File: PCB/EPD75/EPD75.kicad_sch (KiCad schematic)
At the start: 109 parts, among them J1 Conn_01x26, J10 TF_PUSH, J11 Reset, J12 TC2030-USB-NL-DS, J3 RELAY, J4 BTN1, J5 USB-C-Socket-V, J6 BTN2, J7 USB-C-Socket-V, J8 PWR, Q1 BSS138, U2 ESP32-S3-MINI-1, U3 MD8942, U8 G3VM-41GR8

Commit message: Clean up
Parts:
- added R15, R16, R17: 10K, RevK:R_0402, symbol Device:R
- R1: LCSC Part # (none) -> C2771738
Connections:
- net +3.3V: now also R15.1, R16.1, R17.1
- net SDMISO: now also R17.2
- net SDMOSI: now also R16.2
- net SDSCK: now also R15.2

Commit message: Resistors
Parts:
- added R18, R19, R20: 10K, RevK:R_0402, symbol Device:R
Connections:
- net +3.3V: now also R18.1, R19.1, R20.1
- net SDMISO: now also R19.2; no longer R17.2
- net SDSCK: now also R18.2; no longer R15.2
- net SDSS: now also R15.2
- net at J10.1 (DAT2): now also R17.2
- net at J10.8 (DAT1): now also R20.2
- no-connect marks 27 -> 25
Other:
- moved on the sheet: J10, R17

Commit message: Tidy
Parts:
- added R21: 10K, RevK:R_0402, symbol Device:R
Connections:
- net +3.3V: now also R21.1
- net SDCD: now also R21.2
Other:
- moved on the sheet: J10, R15, R16, R17, R18, R19, R20

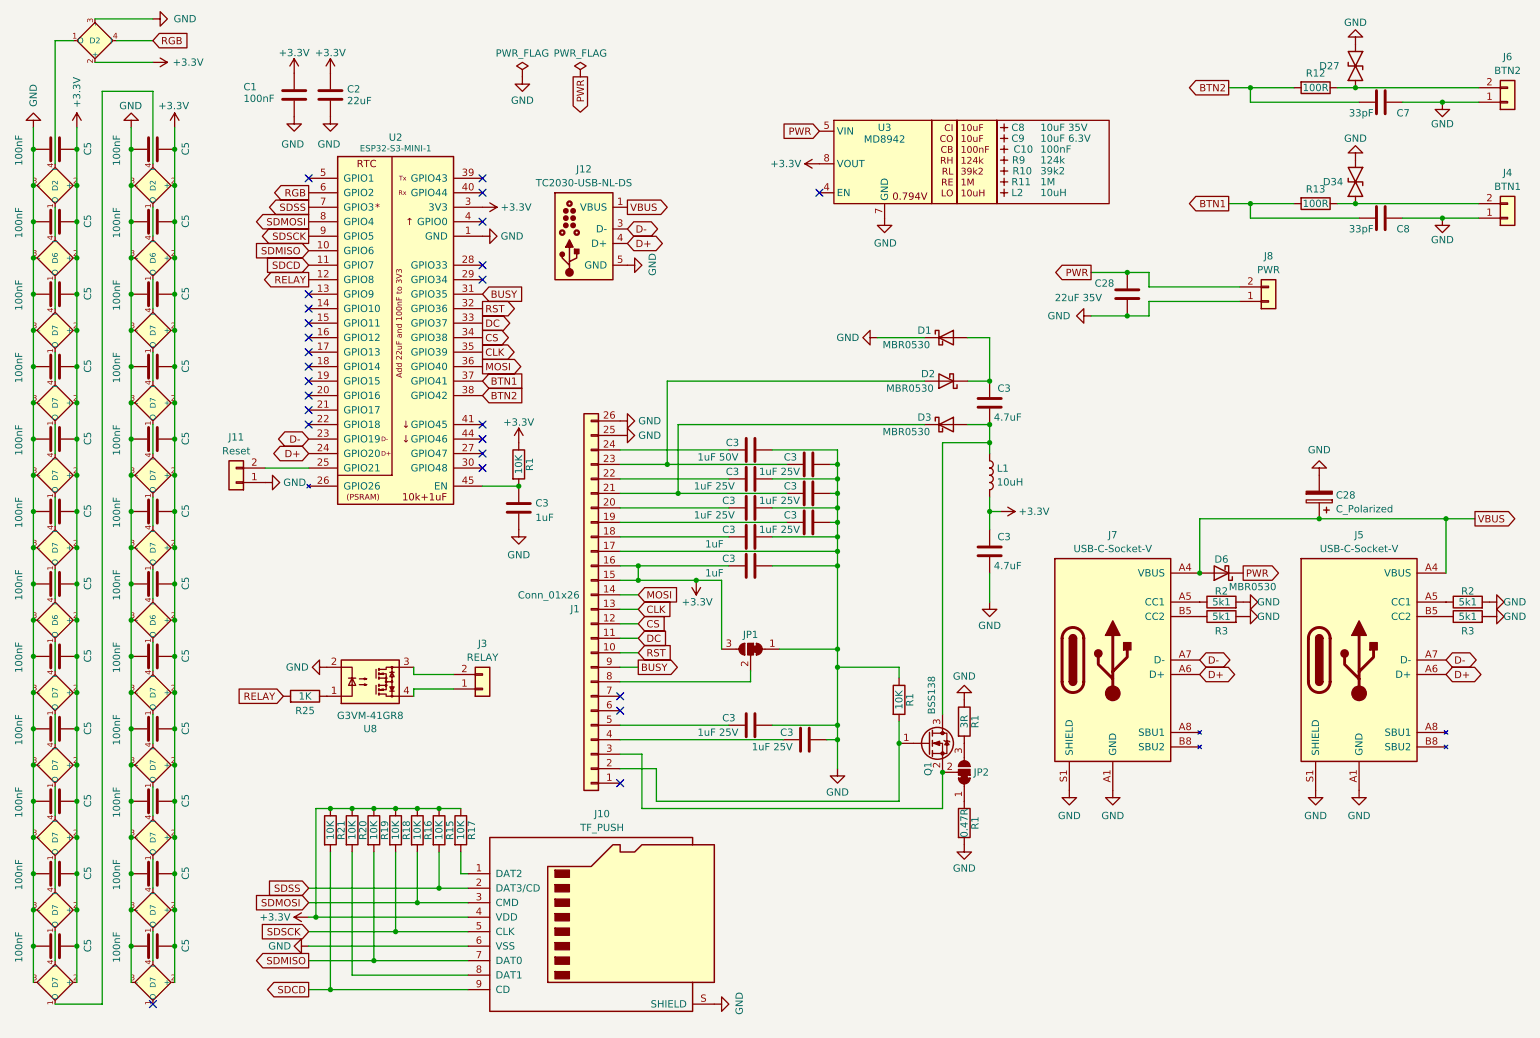
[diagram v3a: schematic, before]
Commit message: New SD card wiring
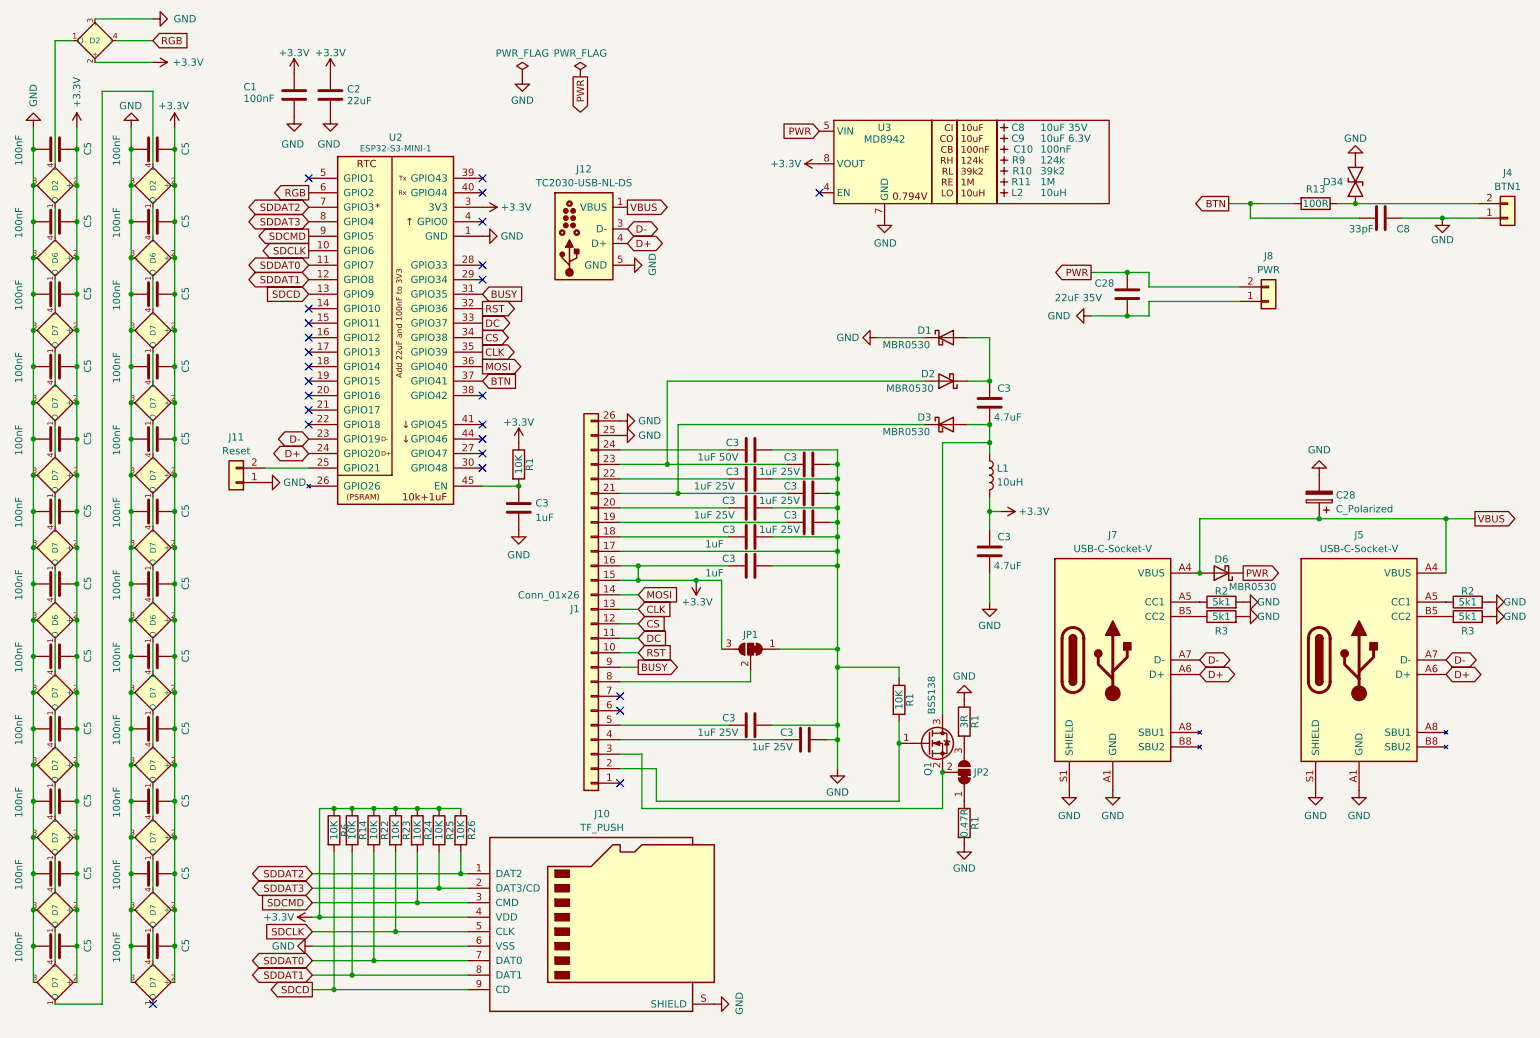
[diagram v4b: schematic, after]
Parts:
- removed C7: 33pF, RevK:C_0402, symbol Device:C
- removed D27: ~, RevK:DFN1006-2L, symbol RevK:ES05D1MC10
- removed J3: RELAY, RevK:WAGO-2060-452-998-404, symbol Connector_Generic:Conn_01x02
- removed J6: BTN2, RevK:WAGO-2060-452-998-404, symbol Connector_Generic:Conn_01x02
- removed R12: 100R, RevK:R_0402, symbol Device:R
- removed R15, R16, R17, R18, R19, R20, R21: 10K, RevK:R_0402, symbol Device:R
- removed U8: G3VM-41GR8, RevK:Special-SOP-4-3.7x4.55, symbol RevK:G3VM-41GR8
- added R14, R22, R23, R24, R26, R6: 10K, RevK:R_0402, symbol Device:R
- R25: value 1K -> 10K
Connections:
- net +3.3V: now also R25.1, R14.1, R22.1, R23.1, R24.1, R26.1, R6.1
- net SDCD: now also U2.13 (GPIO9), R6.2; no longer U2.11 (GPIO7)
- net SDDAT2: now reaches J10.1 (DAT2)
- net SDDAT2: now also U2.7 (GPIO3), R26.2
- net SDDAT1: now reaches J10.8 (DAT1)
- net SDDAT1: now also U2.12 (GPIO8), R14.2
- net BTN1 renamed BTN
- net BTN2: no longer names the net of U2.38 (GPIO42)
- net RELAY renamed SDDAT3
- net SDDAT3: now also J10.2 (DAT3/CD), U2.8 (GPIO4); no longer U2.12 (GPIO8)
- net SDMISO renamed SDCLK
- net SDCLK: now also J10.5 (CLK), R23.2; no longer J10.7 (DAT0)
- net SDMOSI renamed SDCMD
- net SDCMD: now also U2.9 (GPIO5), R24.2; no longer U2.8 (GPIO4)
- removed net SDSCK: J10.5 (CLK), U2.9 (GPIO5)
- removed net SDSS: J10.2 (DAT3/CD), U2.7 (GPIO3)
- new net SDDAT0: J10.7 (DAT0), R22.2, U2.11 (GPIO7)

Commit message: Tidy
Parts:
- D10, D11, D12, D15, D16, D17, D18, D19, D23, D24, D25, D26, D29, D30, D31, D32, D33, D9: renamed from D7; footprint RevK:SMD1010 -> (none); LCSC Part # C5349953 -> (none); MPN (none) -> C5349953
- D14, D22, D28, D8: renamed from D6; footprint RevK:SMD1010 -> (none); LCSC Part # C5349953 -> (none); MPN (none) -> C5349953
- D21, D35, D5: renamed from D2; footprint RevK:SMD1010 -> (none); LCSC Part # C5349953 -> (none); MPN (none) -> C5349953
- D34: LCSC Part # C5137770 -> (none); MPN (none) -> C5137770
- J10: LCSC Part # C393941 -> (none); MPN (none) -> C393941; Position Offset (none) -> 0,0.15
- J5, J7: LCSC Part # C709357 -> (none); MPN (none) -> C709357; Position Offset (none) -> 0,0.715
- Q1: JLCPCB Rotation Offset 180 -> (none); LCSC Part # C2938375 -> (none); MPN (none) -> C2938375; Rotation Offset (none) -> 180
- U3: LCSC Part # C2684786 -> (none); MPN (none) -> C2684786; Rotation Offset (none) -> 180
- U4: renamed from U2; LCSC Part # C3013941 -> (none); MPN (none) -> C3013941
- renumbered C3 to C1, C3 to C11, C3 to C12, C3 to C13, C3 to C14, C3 to C15, C3 to C16, C3 to C17, C3 to C18, C28 to C19, C1 to C2, C5 to C20, C8 to C22, C5 to C23, C5 to C24, C5 to C25, C5 to C26, C5 to C27, C5 to C29, C5 to C30, C5 to C31, C5 to C32, C5 to C33, C5 to C34, C5 to C36, C5 to C37, C5 to C38, C5 to C39, C3 to C4, C5 to C40, C5 to C41, C5 to C43, C5 to C44, C5 to C45, C5 to C46, C5 to C47, C5 to C48, C2 to C5, C3 to C6, C3 to C7, R2 to R12, R3 to R13, R1 to R2, R1 to R3, R2 to R4, R3 to R5, R13 to R7, R1 to R8

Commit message: PCB Update
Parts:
- C28: JLCPCB Rotation Offset 180 -> (none); LCSC Part # C106188 -> (none); MPN (none) -> C106188
- C8: LCSC Part # C194427 -> (none); MPN (none) -> C194427
- C9: LCSC Part # C1691 -> (none); MPN (none) -> C1691
- D1, D2, D3, D6: LCSC Part # C5204746 -> (none); MPN (none) -> C5204746
- J1: LCSC Part # C2856831 -> (none); MPN (none) -> C2856831
- J10: Position Offset 0,0.15 -> (none)
- J4, J8: LCSC Part # C2765055 -> (none); MPN (none) -> C2765055
- J5, J7: Position Offset 0,0.715 -> (none)
- Q1, U3: Rotation Offset 180 -> (none)
- R1: LCSC Part # C2771738 -> (none); MPN (none) -> C2771738
- R9: LCSC Part # C138062 -> (none); MPN (none) -> C138062
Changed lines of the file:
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@@
 			)
 		)
-		(property "Position Offset" "0,0.15"
-			(at 119.38 173.99 0)
-			(effects
-				(font
-					(size 1.27 1.27)
-				)
-				(hide yes)
-			)
-		)
 		(pin "1"
 		)
@@
 			)
 		)
-		(property "LCSC Part #" "C5204746"
+		(property "MPN" "C5204746"
 			(at 228.6 113.665 0)
 			(effects
@@
 			)
 		)
-		(property "LCSC Part #" "C5204746"
+		(property "MPN" "C5204746"
 			(at 180.34 87.63 0)
 			(effects
@@
 			)
 		)
-		(property "LCSC Part #" "C2765055"
+		(property "MPN" "C2765055"
 			(at 236.855 66.04 0)
 			(effects
@@
 			)
 		)
-		(property "LCSC Part #" "C106188"
-			(at 245.745 100.33 0)
-			(effects
-				(font
-					(size 1.27 1.27)
-				)
-				(hide yes)
-			)
-		)
-		(property "JLCPCB Rotation Offset" "180"
+		(property "MPN" "C106188"
 			(at 245.745 100.33 0)
 			(effects
@@
 			)
 		)
-		(property "LCSC Part #" "C138062"
+		(property "MPN" "C138062"
 			(at 190.5 41.275 0)
 			(effects
@@
 			)
 		)
-		(property "LCSC Part #" "C5204746"
+		(property "MPN" "C5204746"
 			(at 180.34 80.01 0)
 			(effects
@@
 			)
 		)
-		(property "LCSC Part #" "C2856831"
+		(property "MPN" "C2856831"
 			(at 118.11 120.015 0)
 			(effects
@@
 			)
 		)
-		(property "Rotation Offset" "180"
-			(at 169.545 41.91 0)
-			(effects
-				(font
-					(size 1.27 1.27)
-				)
-				(hide yes)
-			)
-		)
 		(pin "1"
 		)
@@
 			)
 		)
-		(property "Rotation Offset" "180"
-			(at 177.165 143.51 0)
-			(effects
-				(font
-					(size 1.27 1.27)
-				)
-				(hide yes)
-			)
-		)
 		(pin "1"
 		)
@@
 			)
 		)
-		(property "Position Offset" "0,0.715"
-			(at 252.73 128.905 0)
-			(effects
-				(font
-					(size 1.27 1.27)
-				)
-				(hide yes)
-			)
-		)
 		(pin "A1"
 		)
@@
 			)
 		)
-		(property "LCSC Part #" "C1691"
+		(property "MPN" "C1691"
 			(at 190.5 37.465 0)
 			(effects
@@
 			)
 		)
-		(property "LCSC Part #" "C2771738"
+		(property "MPN" "C2771738"
 			(at 183.515 157.48 90)
 			(effects
@@
 			)
 		)
-		(property "LCSC Part #" "C194427"
+		(property "MPN" "C194427"
 			(at 190.5 35.56 0)
 			(effects
@@
 	)
 	(symbol
-		(lib_name "USB-C-Socket-H_1")
 		(lib_id "RevK:USB-C-Socket-H")
 		(at 209.55 128.905 0)
@@
 			)
 		)
-		(property "Position Offset" "0,0.715"
-			(at 209.55 128.905 0)
-			(effects
-				(font
-					(size 1.27 1.27)
-				)
-				(hide yes)
-			)
-		)
 		(pin "A1"
 		)
@@
 			)
 		)
-		(property "LCSC Part #" "C2765055"
+		(property "MPN" "C2765055"
 			(at 278.765 51.435 0)
 			(effects
@@
 			)
 		)
-		(property "LCSC Part #" "C5204746"
+		(property "MPN" "C5204746"
 			(at 180.34 72.39 0)
 			(effects

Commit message: Model
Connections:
- net D-: now also J12.2 (NC), J12.6 (NC)
- net GND: no longer J12.6 (GND)
- net VBUS: no longer J12.2 (VBUS)
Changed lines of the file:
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@@
 			)
 		)
-		(property "Datasheet" " ~"
+		(property "Datasheet" "~"
 			(at 120.65 55.88 0)
 			(effects

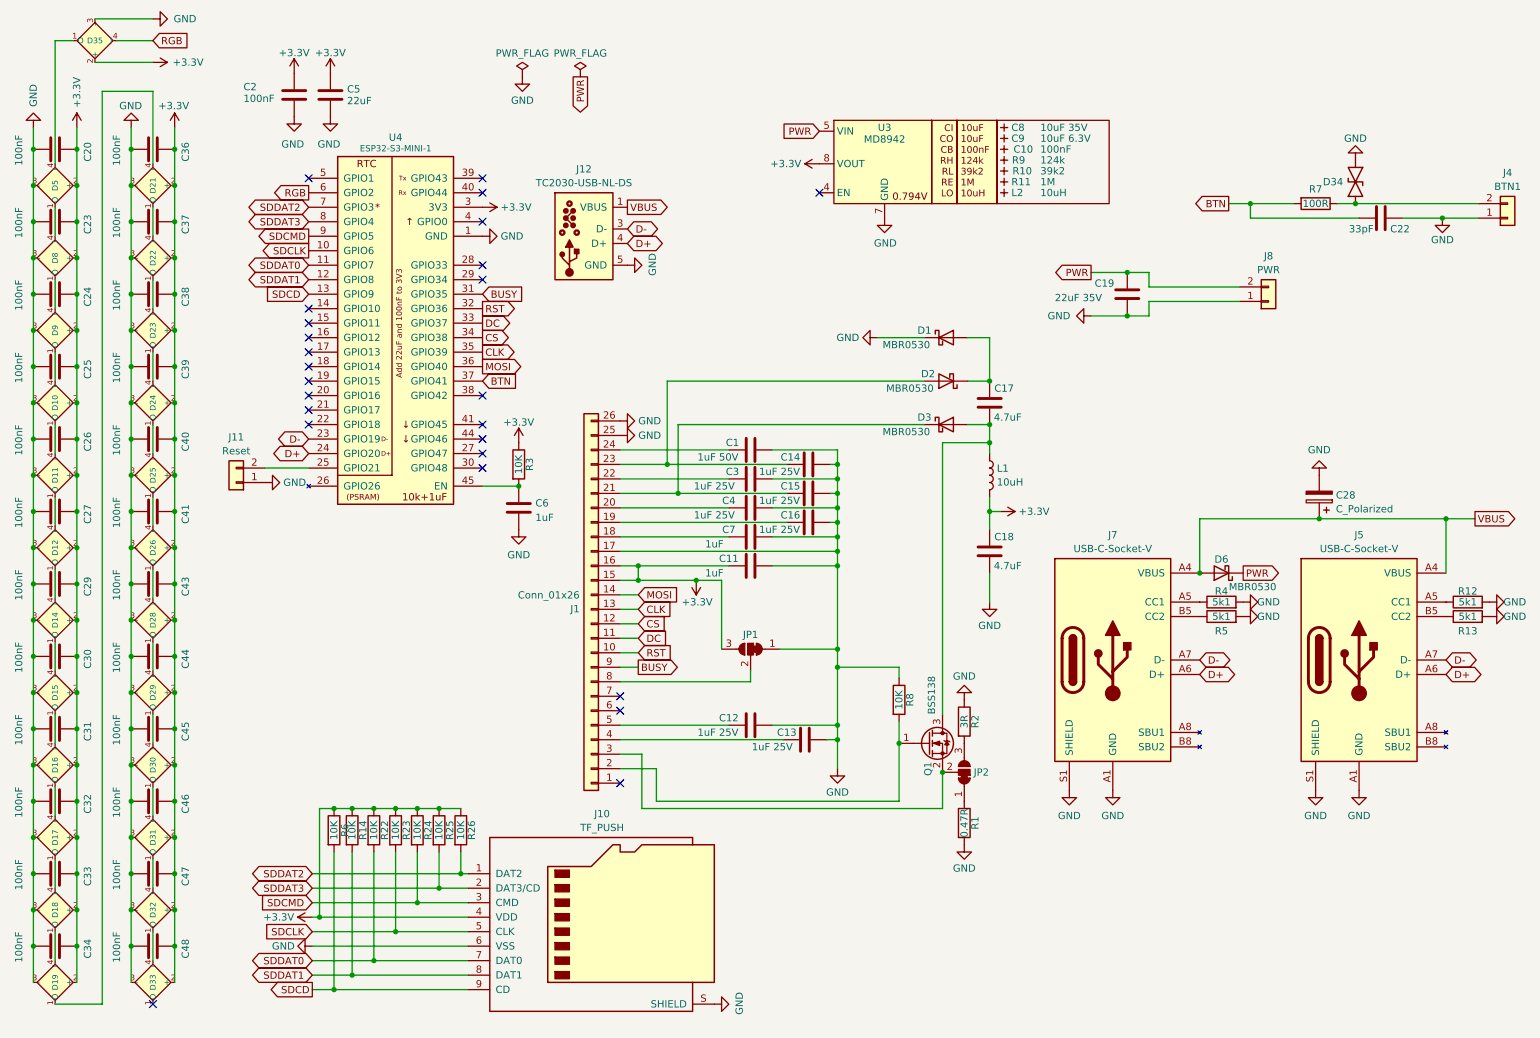
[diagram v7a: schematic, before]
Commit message: Secondary power for e-paper with control.
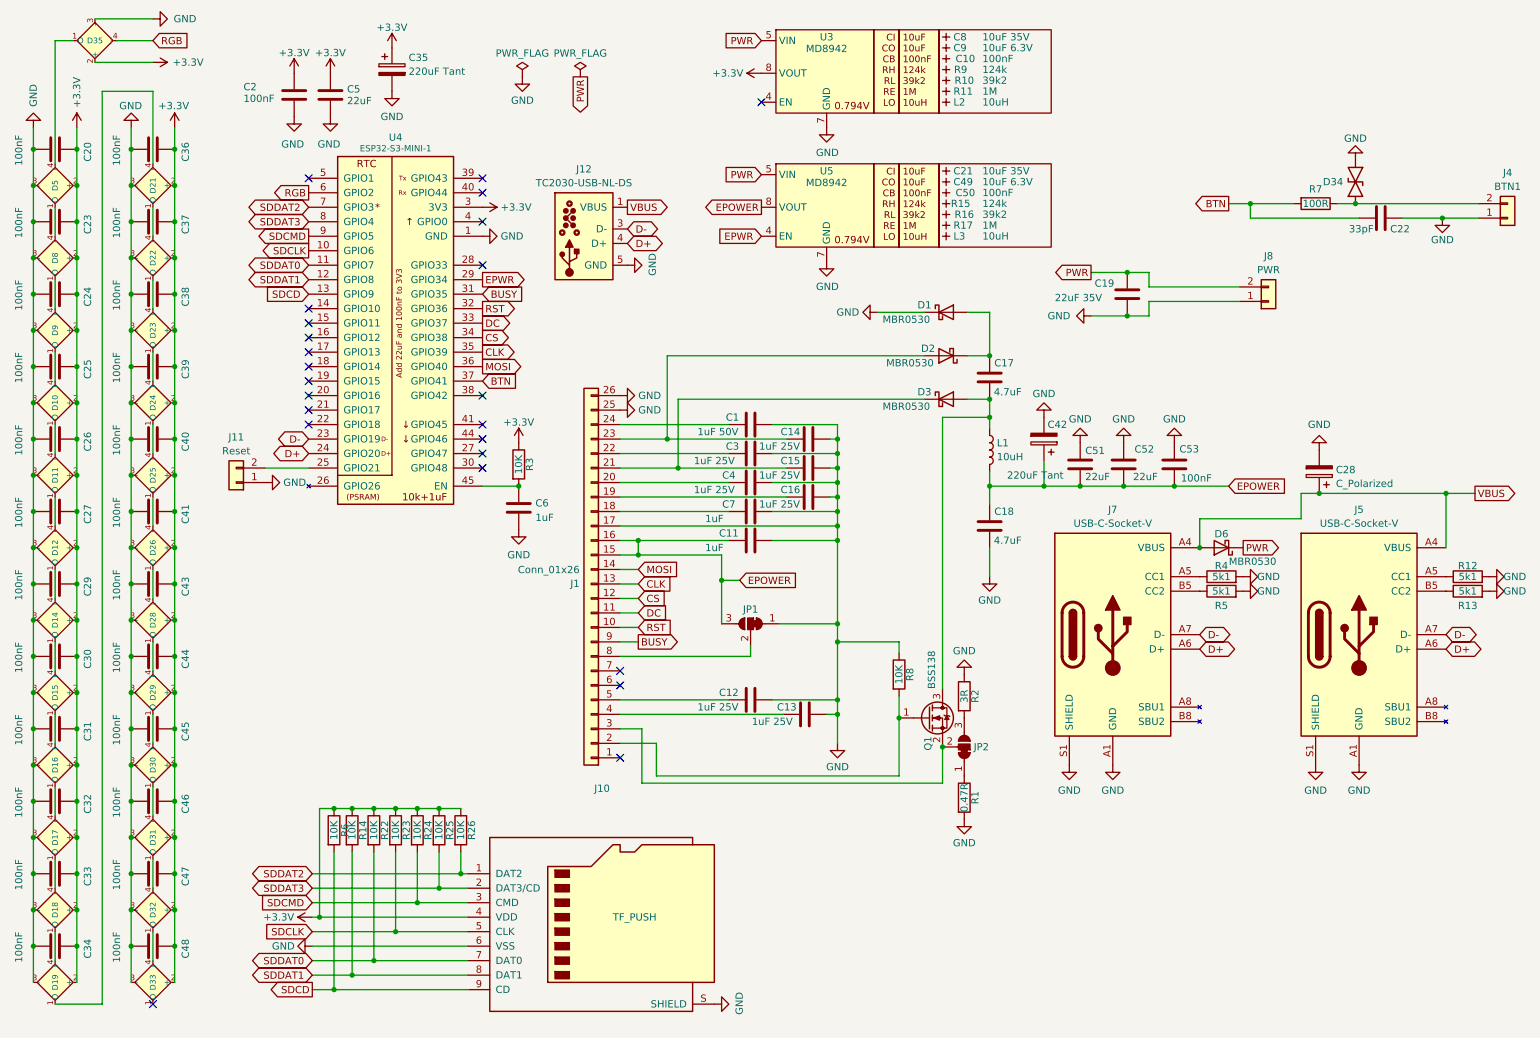
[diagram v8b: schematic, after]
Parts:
- added C21: 10uF 35V, RevK:C_0603_, symbol RevK:Hidden
- added C35, C42: 220uF Tant, RevK:CP_EIA-3528-21_Kemet-B, symbol Device:C_Polarized
- added C49: 10uF 6.3V, RevK:C_0603_, symbol RevK:Hidden
- added C50: 100nF, RevK:C_0603_, symbol RevK:Hidden
- added C51, C52: 22uF, RevK:C_0603, symbol Device:C
- added C53: 100nF, RevK:C_0402, symbol Device:C
- added L3: 10uH, RevK:L_4x4_, symbol RevK:Hidden
- added R15: 124k, RevK:R_0402_, symbol RevK:Hidden
- added R16: 39k2, RevK:R_0402_, symbol RevK:Hidden
- added R17: 1M, RevK:R_0402_, symbol RevK:Hidden
- added U5: MD8942, RevK:SOT-23-6-MD8942, symbol RevK:MD89420-RegBlock
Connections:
- net +3.3V: now also C35.1; no longer C11.1, C18.2, J1.15 (Pin_15), J1.16 (Pin_16), JP1.3 (B), L1.2
- net GND: now also C35.2, C42.2, C51.1, C52.1, C53.1, U5.2 (GND), U5.7 (GND)
- net PWR: now also U5.5 (VIN)
- net EPWR: now reaches U4.29 (GPIO34)
- net EPWR: now also U5.4 (EN)
- new net EPOWER: C11.1, C18.2, C42.1, C51.2, C52.2, C53.2, J1.15 (Pin_15), J1.16 (Pin_16), JP1.3 (B), L1.2, U5.8 (VOUT)
- no-connect marks 25 -> 24
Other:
- moved on the sheet: C1, C10, C11, C12, C13, C14, C15, C16, C17, C18, C28, C3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
